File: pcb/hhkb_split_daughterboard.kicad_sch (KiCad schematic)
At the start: 3 parts

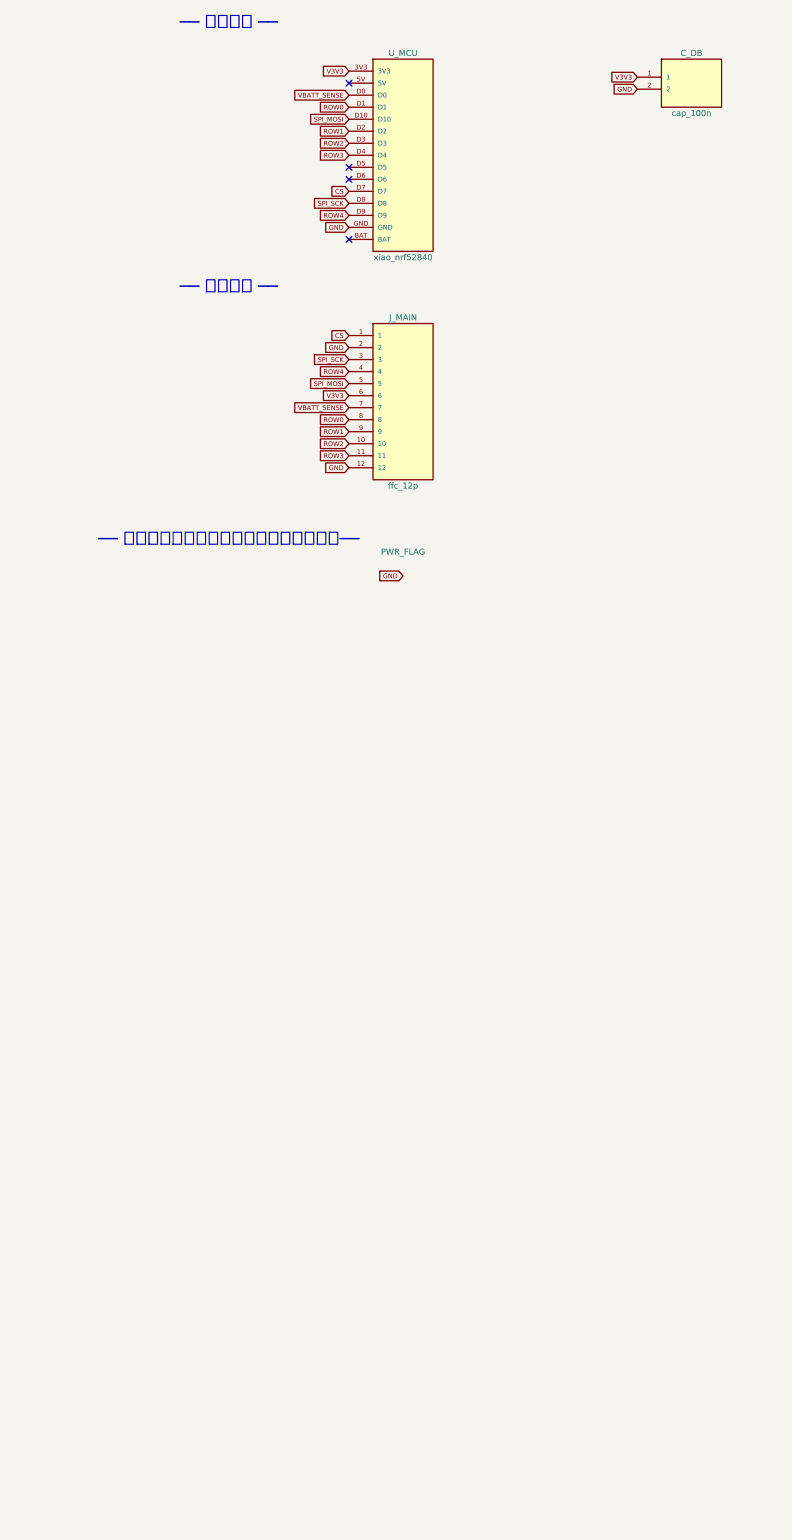
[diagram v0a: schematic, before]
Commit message: 回路図のバス配線を「部品ごとに枝を引く」方式に固め、可読性の指摘に応えた（指摘1）
同じネット（V3V3・GND）を1本のバスから各部品へ枝で配る方式に、
以下の防御を加えて安定させた。

- 枝は「先に横、それから縦」で描き、ピンの列を素通りしない
  （同じ部品が V3V3・GND を両方持つ場合、隣接ピンを串刺しにして
  無関係なネットに誤統合される事故が3回起きた）
- バスの枝は全部品を置き終えたあとに一括で描く
  （グループの処理順に依存する短絡を避ける）
- ピンピッチを 2.54mm→5.08mm に広げ、グローバルラベルの矢印が
  隣どうしで重ならないようにした（1.27mmグリッドの整数倍を維持）

利用者のスクリーンショット指摘（上下バスが同じ足につながって見える・
V3V3ラベルとCOL0ラベルの文字が重なる）を実測で確認し、解消した。

確認: test_schematic.py 9件全通過。ERC の multiple_net_names・
pin_to_pin エラーは複数回の再生成で0件。netlist の最大ノードは
GND=12（以前は69ノードの巨大ネット化バグがあった）。
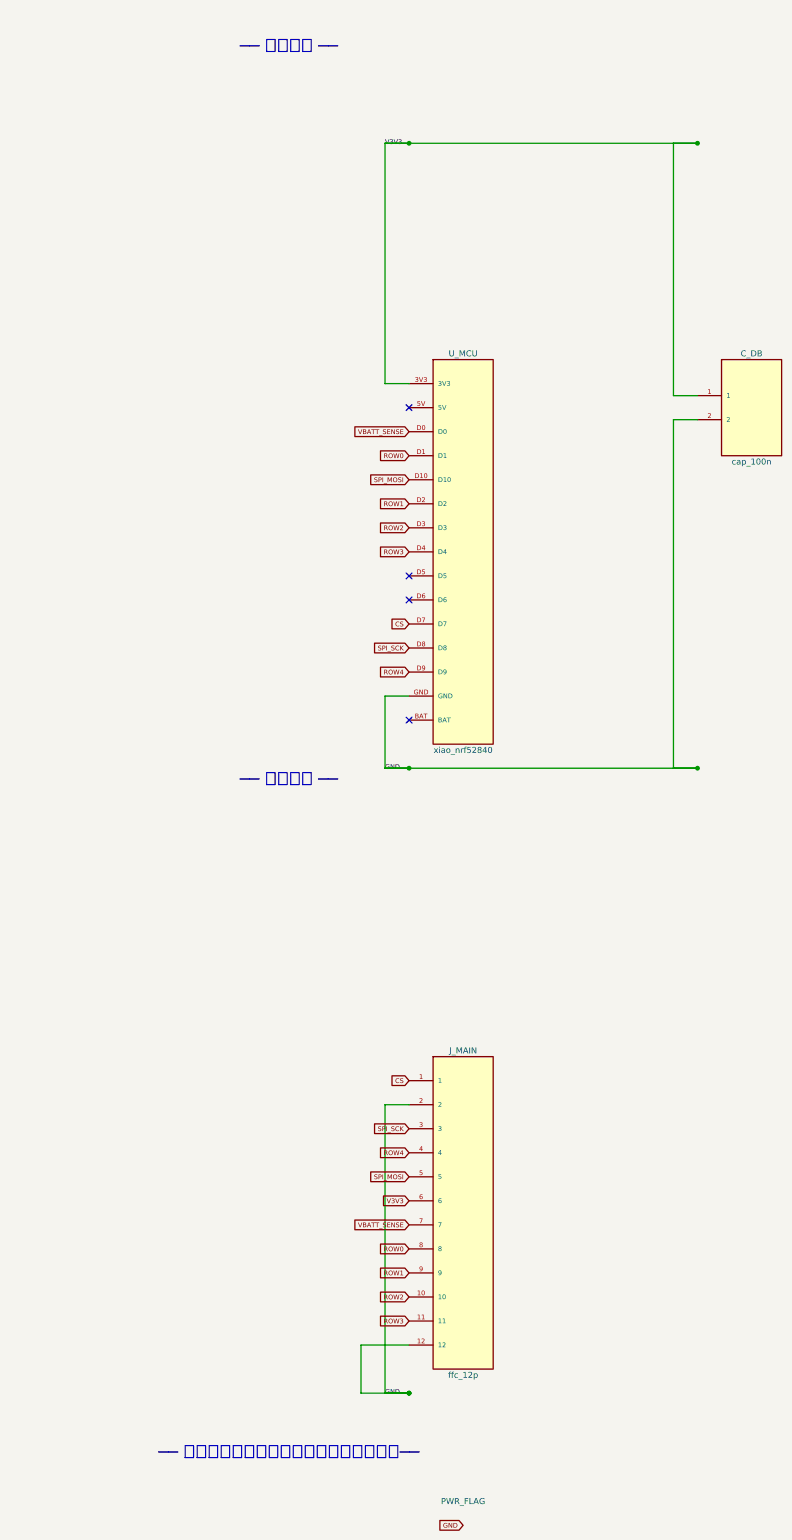
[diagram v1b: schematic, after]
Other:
- moved on the sheet: C_DB, J_MAIN, U_MCU
